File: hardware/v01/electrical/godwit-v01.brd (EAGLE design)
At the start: 72.5 x 132.8 mm, 95 parts, among them J1 USB-MINIB-M26FTR, U1 BQ24251, U2 LM3668-3034, U3 UC530, U4 AAT4280A, U5 BMP180, U6 MAG3110, U7 ATUCL4U-TQFP48

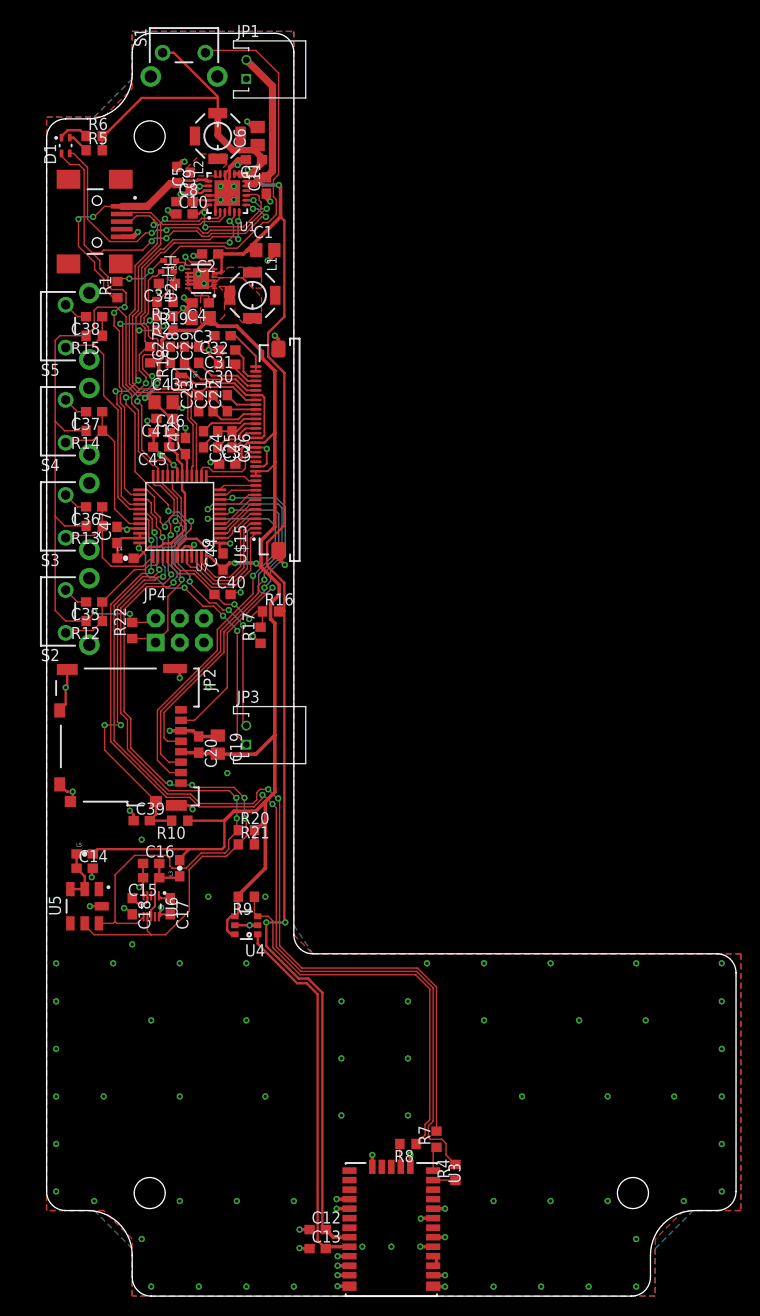
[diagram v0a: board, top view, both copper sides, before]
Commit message: Spun sd card right way and rerouted...
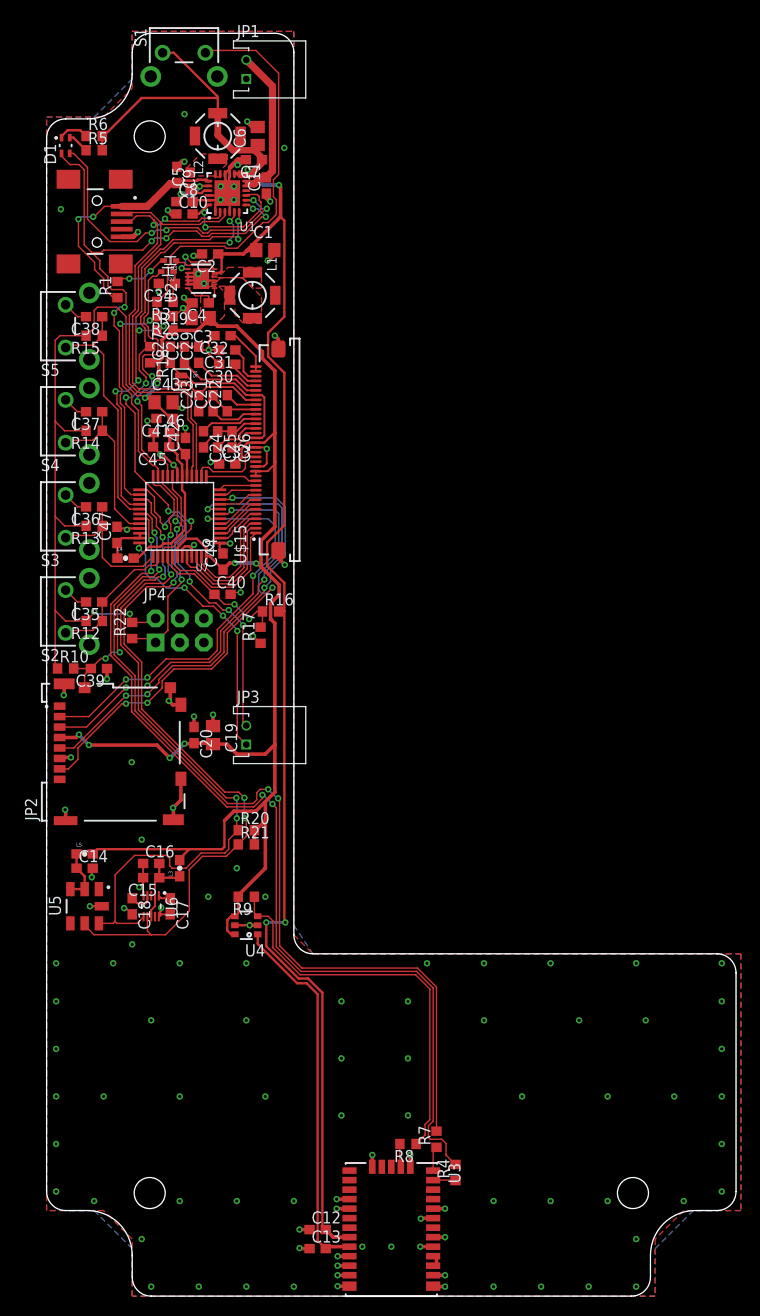
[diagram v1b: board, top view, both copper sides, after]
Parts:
- moved R10 20.0 mm to (2.00, 66.0), turned to 0 degrees
- moved JP2 19.7 mm to (2.00, 50.0), turned to 90 degrees
- moved C39 16.6 mm to (5.50, 66.0), turned to 180 degrees
- moved C19 1.12 mm to (17.5, 59.0)
- moved C20 1.12 mm to (15.5, 59.0)
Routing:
- net 3.0V: track 235.4 -> 252.3 mm, vias 6 -> 10
- net SD_CRD_DET: track 45.0 -> 28.6 mm
- net SD_MISO: track 36.0 -> 50.0 mm, vias 2 -> 4
- net SD_SCLK: track 38.9 -> 47.0 mm, vias 2 -> 4
- net SD_MOSI: track 43.1 -> 47.4 mm, vias 2 -> 4
- net GPS_RX: track 98.3 -> 95.1 mm
- net GPS_TX: track 101.7 -> 98.5 mm
- net SENS_SDA: track 78.2 -> 75.1 mm
- net SENS_SCL: track 78.3 -> 75.2 mm, vias 6 -> 4
- net GND: track 138.6 -> 136.0 mm, vias 122 -> 127
- net SD_!CS!: track 41.5 -> 43.7 mm, vias 2 -> 4

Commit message: Finished EagleUp
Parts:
- U6: device hybridpi-sensor:DFN-10 -> hybridpi-sensor:DFN-10-2X2
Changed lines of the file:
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@@
 <setting verticaltext="up"/>
 </settings>
-<grid distance="1" unitdist="mm" unit="mm" style="lines" multiple="1" display="yes" altdistance="0.05" altunitdist="mm" altunit="mm"/>
+<grid distance="0.05" unitdist="inch" unit="mm" style="lines" multiple="1" display="yes" altdistance="0.005" altunitdist="inch" altunit="inch"/>
 <layers>
 <layer number="1" name="Top" color="4" fill="1" visible="yes" active="yes"/>
@@
 <layer number="220" name="220bmp" color="21" fill="1" visible="no" active="no"/>
 <layer number="221" name="221bmp" color="22" fill="1" visible="no" active="no"/>
-<layer number="222" name="222bmp" color="23" fill="1" visible="no" active="no"/>
 <layer number="223" name="223bmp" color="24" fill="1" visible="no" active="no"/>
 <layer number="224" name="224bmp" color="25" fill="1" visible="no" active="no"/>
@@
 <element name="L2" library="hybridpi" package="SRU5028" value="1uH" x="18" y="122" rot="R90"/>
 <element name="U1" library="hybridpi" package="VQFN-24" value="BQ24251" x="19" y="116" rot="R180"/>
-<element name="U2" library="hybridpi" package="WSON-12" value="LM3668-3034" x="16.25" y="107" rot="R90"/>
+<element name="U2" library="hybridpi" package="WSON-12" value="LM3668-3034" x="16.25" y="107" rot="R90">
+<attribute name="EAGLEUP" value="WSON-12-3p1x3p1" x="16.25" y="107" size="1.778" layer="27" rot="R90" display="off"/>
+</element>
 <element name="C1" library="hybridpi-rcl" package="C0805" value="10uF" x="23" y="110">
 <attribute name="VENDOR" value="DIGI-KEY" x="91.58" y="61.74" size="1.778" layer="27" display="off"/>
@@
 <element name="R5" library="hybridpi-rcl" package="R0603" value="2.2K" x="5" y="120.5"/>
 <element name="R6" library="hybridpi-rcl" package="R0603" value="2.2K" x="5" y="122"/>
-<element name="D1" library="hybridpi-opto" package="LED-2-1.6X1.25" value="LED-RG-APT" x="2" y="121" rot="R90"/>
+<element name="D1" library="hybridpi-opto" package="LED-2-1.6X1.25" value="LED-RG-APT" x="2" y="121" rot="R90">
+<attribute name="EAGLEUP" value="LED-1p6x1p25" x="2" y="121" size="1.778" layer="27" rot="R90" display="off"/>
+</element>
 <element name="JP1" library="hybridpi-connector" package="JST-PH-2-RA" value="M02-JST-PH-2-RA" x="21" y="129" rot="R270">
 <attribute name="EAGLEUP" value="JST-PH-2-RA" x="21" y="129" size="1.778" layer="27" rot="R270" display="off"/>
@@
 <element name="D3" library="hybridpi-discrete-semi" package="SOD523" value="" x="13" y="108.9" rot="R180"/>
 <element name="R1" library="hybridpi-rcl" package="R0603" value="100K" x="7.45" y="105.85" rot="R90"/>
-<element name="U3" library="hybridpi-rf" package="UC530" value="UC530" x="36.25" y="7" rot="R270"/>
+<element name="U3" library="hybridpi-rf" package="UC530" value="UC530" x="36.25" y="7" rot="R270">
+<attribute name="EAGLEUP" value="UC530" x="36.25" y="7" size="1.778" layer="27" rot="R270" display="off"/>
+</element>
 <element name="C12" library="hybridpi-rcl" package="C0603" value="1uF" x="28.5" y="7">
 <attribute name="VOLTAGE" value="&gt;=10V" x="60.25" y="-70.47" size="1.778" layer="27" display="off"/>
@@
 </element>
 <element name="R9" library="hybridpi-rcl" package="R0603" value="100K" x="21" y="42" rot="R180"/>
-<element name="U5" library="hybridpi-sensor" package="BMP180" value="BMP180" x="4" y="41"/>
+<element name="U5" library="hybridpi-sensor" package="BMP180" value="BMP180" x="4" y="41">
+<attribute name="EAGLEUP" value="BMP180" x="4" y="41" size="1.778" layer="27" display="off"/>
+</element>
 <element name="C14" library="hybridpi-rcl" package="C0603" value="0.1uF" x="4" y="45"/>
-<element name="U6" library="hybridpi-sensor" package="DFN-10" value="MAG3110" x="11" y="41" rot="R270"/>
+<element name="U6" library="hybridpi-sensor" package="DFN-10-2X2" value="MAG3110" x="11" y="41" rot="R270">
+<attribute name="EAGLEUP" value="DFN-10-2x2" x="11" y="41" size="1.778" layer="27" rot="R270" display="off"/>
+</element>
 <element name="C15" library="hybridpi-rcl" package="C0603" value="0.1uF" x="11" y="44" rot="R180"/>
 <element name="C16" library="hybridpi-rcl" package="C0603" value="1uF" x="11" y="45.5">
@@
 <attribute name="VENDOR_PN" value="587-1248-1-ND" x="50.75" y="4.95" size="1.778" layer="27" display="off"/>
 </element>
-<element name="U7" library="hybridpi-digitalic" package="TQFP48" value="ATUCL4U-TQFP48" x="14" y="82" rot="R180"/>
+<element name="U7" library="hybridpi-digitalic" package="TQFP48" value="ATUCL4U-TQFP48" x="14" y="82" rot="R180">
+<attribute name="EAGLEUP" value="TQFP-48" x="14" y="82" size="1.778" layer="27" rot="R180" display="off"/>
+</element>
 <element name="R12" library="hybridpi-rcl" package="R0603" value="100K" x="5" y="71" rot="R180"/>
 <element name="R13" library="hybridpi-rcl" package="R0603" value="100K" x="5" y="81" rot="R180"/>
@@
 <attribute name="VENDOR_PN" value="587-1893-1-ND" x="19.24" y="-41.13" size="1.778" layer="27" display="off"/>
 </element>
-<element name="JP4" library="hybridpi-connector" package="2X3-NS" value="" x="14" y="70"/>
+<element name="JP4" library="hybridpi-connector" package="2X3-NS" value="" x="14" y="70">
+<attribute name="EAGLEUP" value="M03X2" x="14" y="70" size="1.778" layer="27" display="off"/>
+</element>
 <element name="R22" library="hybridpi-rcl" package="R0603" value="10K" x="9" y="70" rot="R90"/>
 <element name="SJ1" library="hybridpi-passive" package="SJ_2S" value="SOLDERJUMPERNC" x="14.15" y="96.4" rot="R270"/>
@@
 <wire x1="17.4" y1="58.15" x2="17.5" y2="58.05" width="0.381" layer="1"/>
 <wire x1="17.5" y1="58.05" x2="18.95" y2="58.05" width="0.381" layer="1"/>
-<wire x1="18.95" y1="58.05" x2="20" y2="57" width="0.381" layer="1"/>
-<wire x1="20" y1="57" x2="23" y2="57" width="0.381" layer="1"/>
-<wire x1="23" y1="57" x2="24" y2="58" width="0.381" layer="1"/>
+<wire x1="22.85" y1="56.85" x2="24" y2="58" width="0.381" layer="1"/>
 <via x="12.95" y="56.6" extent="1-16" drill="0.3302"/>
 <via x="14.5" y="58.1" extent="1-16" drill="0.3302"/>
@@
 <wire x1="4.45" y1="57.95" x2="11.6" y2="57.95" width="0.381" layer="1"/>
 <wire x1="11.6" y1="57.95" x2="12.95" y2="56.6" width="0.381" layer="1"/>
+<wire x1="18.95" y1="58.05" x2="20.15" y2="56.85" width="0.381" layer="1"/>
+<wire x1="20.15" y1="56.85" x2="22.85" y2="56.85" width="0.381" layer="1"/>
 </signal>
 <signal name="N$3">
@@
 <wire x1="22.479" y1="117.602" x2="23.052" y2="117.602" width="0.762" layer="1"/>
 <wire x1="23.052" y1="117.602" x2="23.1" y2="117.65" width="0.762" layer="1"/>
-<wire x1="23.749" y1="127.251" x2="23.749" y2="118.299" width="0.762" layer="1"/>
+<wire x1="23.749" y1="127.651" x2="23.749" y2="118.299" width="0.762" layer="1"/>
 <wire x1="23.749" y1="118.299" x2="23.1" y2="117.65" width="0.762" layer="1"/>
-<wire x1="23.749" y1="127.251" x2="21" y2="130" width="0.764" layer="1"/>
+<wire x1="23.749" y1="127.651" x2="21.4" y2="130" width="0.762" layer="1"/>
+<wire x1="21.4" y1="130" x2="21" y2="130" width="0.762" layer="1"/>
 </signal>
 <signal name="LDO">

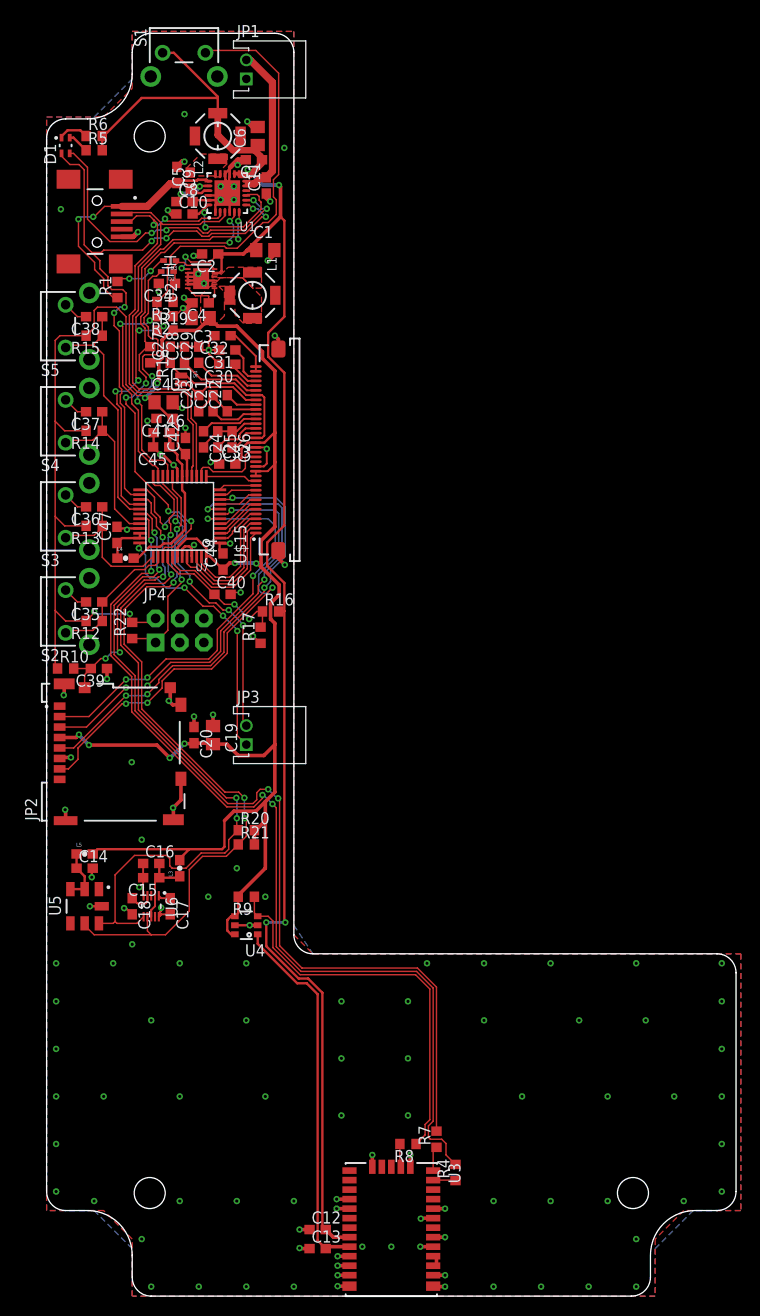
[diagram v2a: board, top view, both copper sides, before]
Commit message: Added current limiting resistors and finalized v01 design.
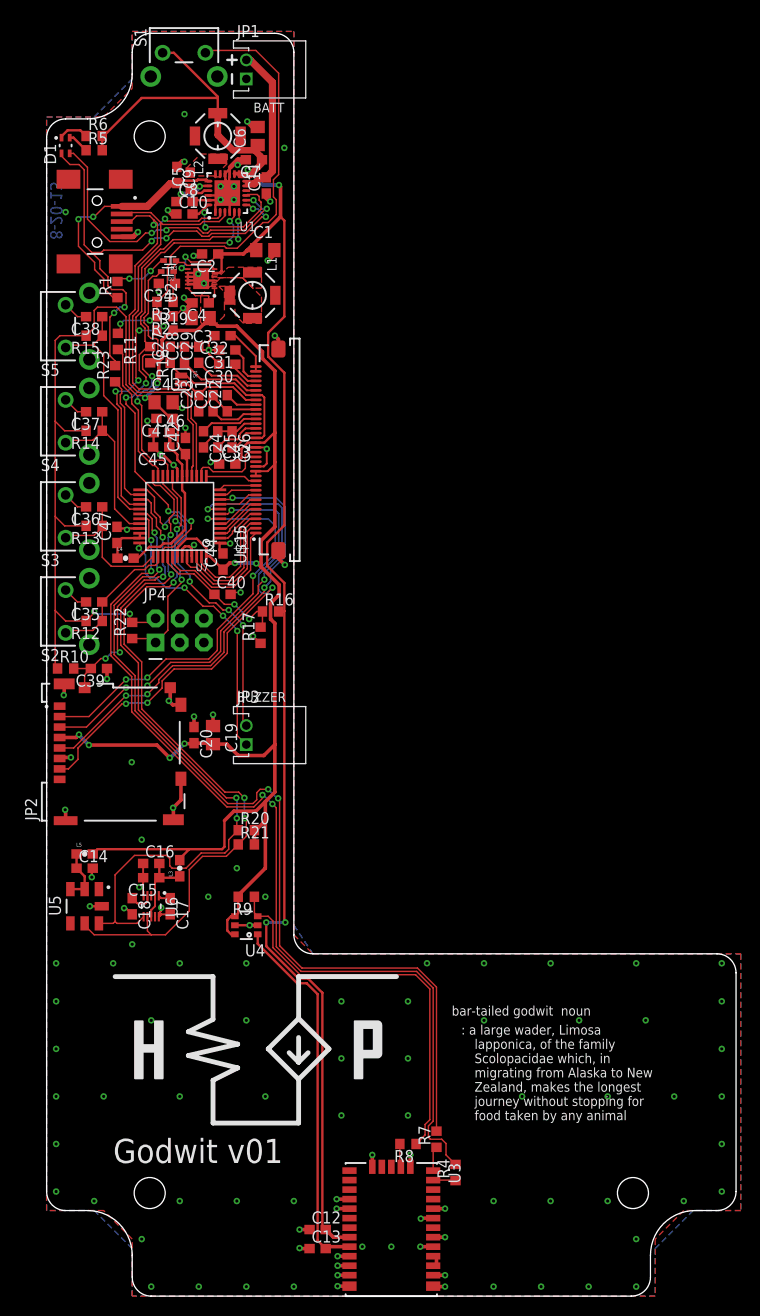
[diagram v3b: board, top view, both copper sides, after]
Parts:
- added R11, R23: 100K, hybridpi-rcl:R0603
- added U$21: (no value), hybridpi-aesthetics:LOGO_MED_SLK
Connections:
- net !PG! renamed !PG!_LED
- new net N$88: R11.1, R2.2, R3.2, S1.1
- new net STAT_LED: D1.2, R23.2, U1.7
- net CHRG_STAT: now also R23.1; no longer D1.2, U1.7
- net PWR_TACT: now also R11.2; no longer R2.2, R3.2, S1.1
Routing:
- net CHRG_STAT: track 65.4 -> 13.6 mm, vias 6 -> 0
- net PWR_TACT: track 66.0 -> 15.3 mm, vias 2 -> 0
- net STAT_LED: track 0.00 -> 50.4 mm, vias 0 -> 6
- net N$88: track 0.00 -> 49.3 mm, vias 0 -> 2
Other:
- board text added: "8-20-13"
- board text added: ": a large wader, Limosa"
- board text added: "BATT"
- board text added: "BUZZER"
- board text added: "Godwit v01"
- board text added: "LCD"
- board text added: "Scolopacidae which, in"
- board text added: "Zealand, makes the longest"
- board text added: "bar-tailed godwit noun"
- board text added: "food taken by any animal"
- board text added: "journey without stopping for"
- board text added: "lapponica, of the family"
- board text added: "migrating from Alaska to New"

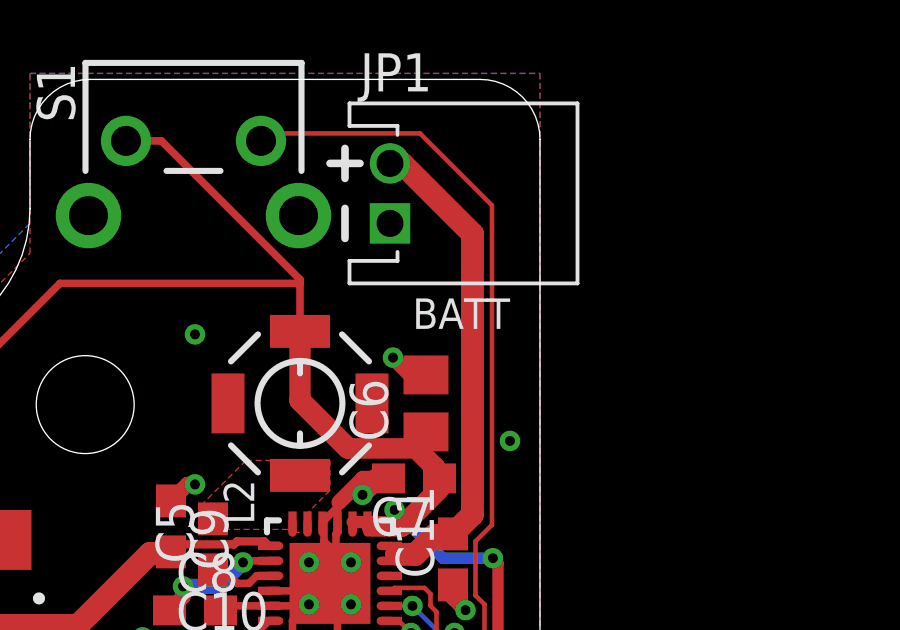
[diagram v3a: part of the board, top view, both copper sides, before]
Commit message: panelized and gerbered.
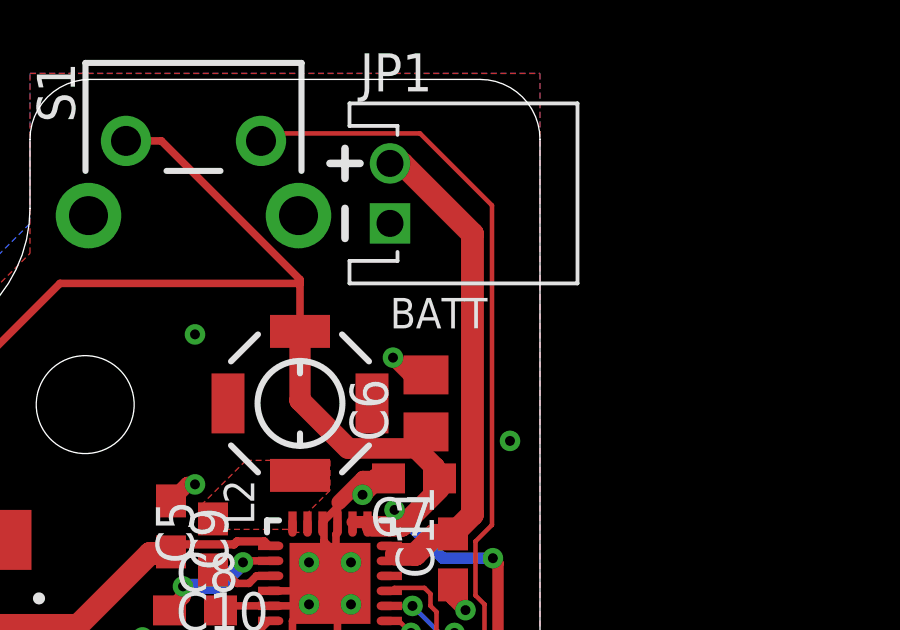
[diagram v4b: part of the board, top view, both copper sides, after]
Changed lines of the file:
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@@
 <layer number="39" name="tKeepout" color="4" fill="11" visible="no" active="yes"/>
 <layer number="40" name="bKeepout" color="1" fill="11" visible="no" active="yes"/>
-<layer number="41" name="tRestrict" color="4" fill="10" visible="yes" active="yes"/>
-<layer number="42" name="bRestrict" color="1" fill="10" visible="yes" active="yes"/>
+<layer number="41" name="tRestrict" color="4" fill="10" visible="no" active="yes"/>
+<layer number="42" name="bRestrict" color="1" fill="10" visible="no" active="yes"/>
 <layer number="43" name="vRestrict" color="2" fill="10" visible="no" active="yes"/>
 <layer number="44" name="Drills" color="7" fill="1" visible="no" active="yes"/>
@@
 <text x="20" y="62.5" size="1.016" layer="21" font="vector" ratio="15">BUZZER</text>
 <text x="21" y="78" size="1.016" layer="21" font="vector" ratio="15" rot="R90">LCD</text>
-<text x="25" y="125.5" size="1.016" layer="21" font="vector" ratio="15" rot="R180">BATT</text>
+<text x="21" y="124.5" size="1.016" layer="21" font="vector" ratio="15">BATT</text>
 <wire x1="19" y1="130" x2="20" y2="130" width="0.254" layer="21"/>
 <wire x1="19.5" y1="130.5" x2="19.5" y2="129.5" width="0.254" layer="21"/>
@@
 </signal>
 </signals>
-<errors>
-</errors>
 </board>
 </drawing>
